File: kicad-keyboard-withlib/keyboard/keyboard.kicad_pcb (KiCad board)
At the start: 2 copper layers, 149.1 x 131.9 mm, 92 parts, among them SW1 SW_Push, SW10 SW_Push, SW11 SW_Push, SW12 SW_Push, SW13 SW_Push, SW14 SW_Push, SW15 SW_Push, SW16 SW_Push, SW17 SW_Push, SW18 SW_Push, SW19 SW_Push, SW2 SW_Push, SW20 SW_Push, SW21 SW_Push, SW22 SW_Push, SW23 SW_Push, SW24 SW_Push, SW25 SW_Push, SW26 SW_Push, SW27 SW_Push, SW28 SW_Push, SW29 SW_Push, SW3 SW_Push, SW30 SW_Push, SW31 SW_Push, SW32 SW_Push, SW33 SW_Push, SW34 SW_Push, SW35 SW_Push, SW36 SW_Push, SW37 SW_Push, SW38 SW_Push, SW39 SW_Slide_DPDT, SW4 SW_Push, SW5 SW_Push, SW6 SW_Push, SW7 SW_Push, SW8 SW_Push, SW9 SW_Push, U2 MCP23017_SO

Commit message: add:keyboardpcb almost done missing holes and homemade frogs
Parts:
- moved D30 160.6 mm to (153.0, 81.7)
- moved D38 158.6 mm to (152.2, 102.1)
- moved D19 152.4 mm to (132.6, 100.7)
- moved D20 148.1 mm to (132.6, 103.1)
- moved D18 145.6 mm to (121.4, 100.7)
- moved D17 138.4 mm to (109.8, 100.7)
- moved D28 137.1 mm to (120.2, 122.7)
- moved D29 133.4 mm to (120.4, 125.3)
- moved D27 130.9 mm to (109.6, 122.1)
- moved D36 130.2 mm to (110.2, 142.9)
- moved D37 126.8 mm to (110.2, 146.1)
- moved D26 123.9 mm to (98.0, 122.1)
- moved D35 123.4 mm to (98.8, 142.7)
- moved D25 117.1 mm to (86.8, 121.9)
- moved D34 116.9 mm to (87.6, 142.7)
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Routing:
- net Net-(U1-R1): track 175.9 -> 146.6 mm
- net Net-(U2-GPA5): track 25.9 -> 0.00 mm
- net Net-(U1-R4): track 246.4 -> 257.5 mm
- net Net-(D20-Pad1): track 0.00 -> 8.71 mm
- net Net-(D34-Pad1): track 0.00 -> 8.05 mm
- net Net-(D36-Pad1): track 0.00 -> 7.93 mm
- net Net-(D32-Pad1): track 0.00 -> 7.93 mm
- net Net-(D27-Pad1): track 0.00 -> 7.93 mm
- net Net-(D24-Pad1): track 0.00 -> 7.93 mm
- net Net-(D29-Pad1): track 0.00 -> 7.89 mm, vias 0 -> 2
- net Net-(D16-Pad1): track 0.00 -> 7.86 mm
- net Net-(D15-Pad1): track 0.00 -> 7.86 mm
- net Net-(D14-Pad1): track 0.00 -> 7.86 mm
- net Net-(D13-Pad1): track 0.00 -> 7.86 mm
- net Net-(D12-Pad1): track 0.00 -> 7.86 mm
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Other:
- board text added: "LLECIAK, MPETITCO, NROBINSO"
- board text removed: "APETITCO, LLECIAK, NROBINSO"

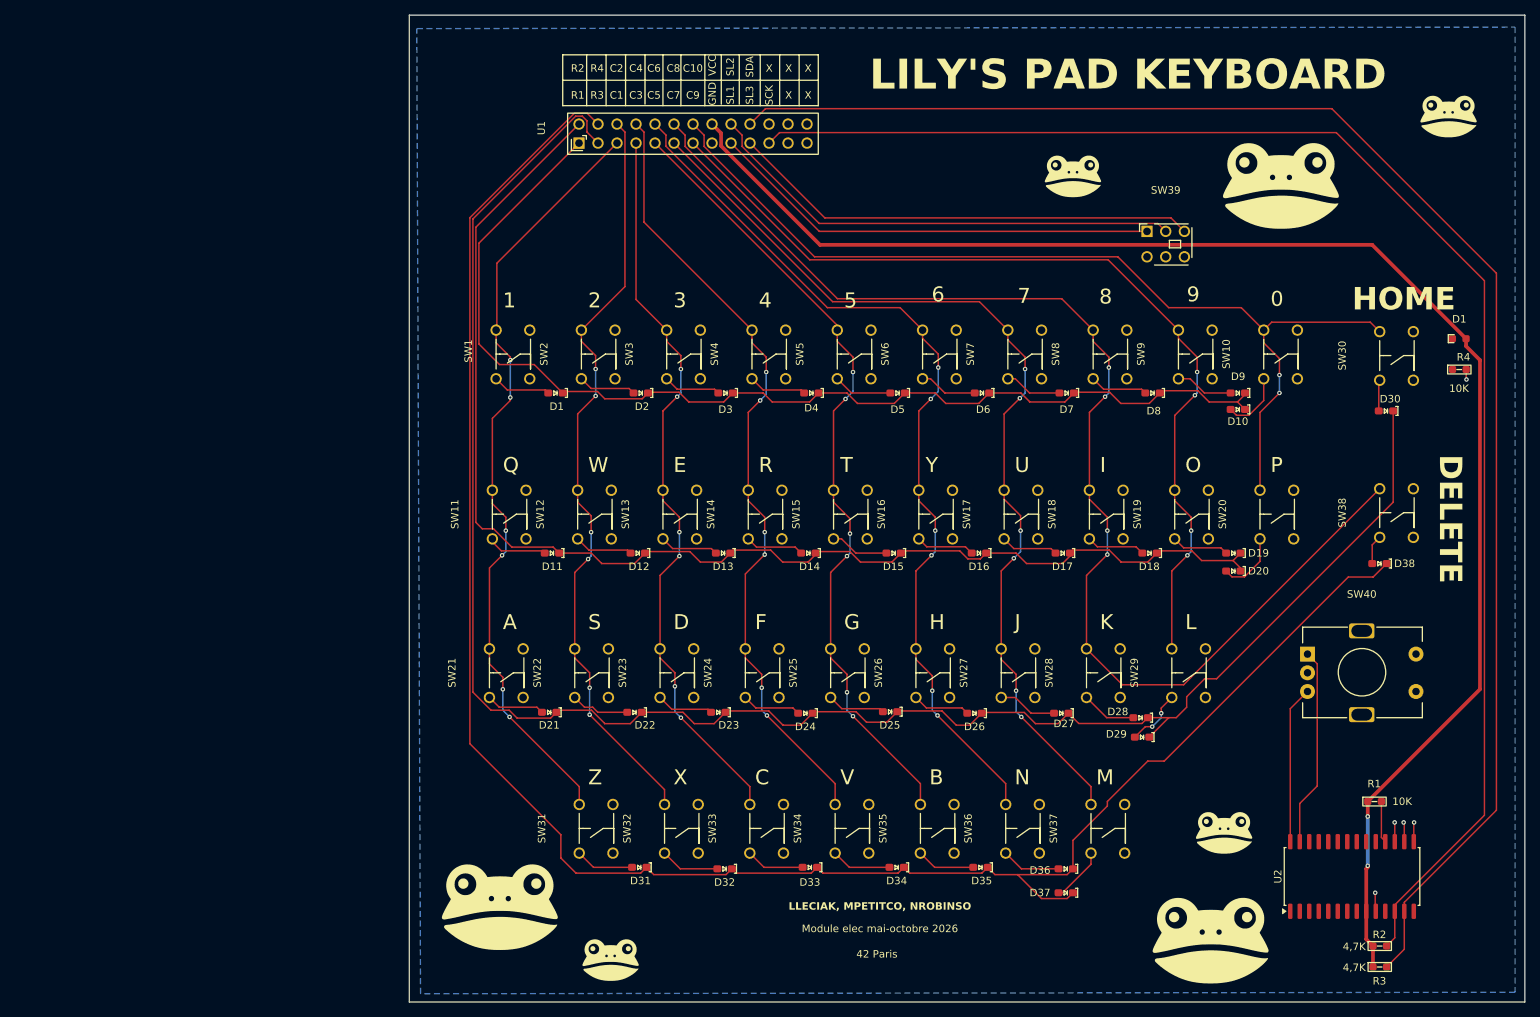
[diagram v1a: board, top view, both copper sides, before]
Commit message: add: holes in the corner of the keyboard pcb, missing homemade frogs
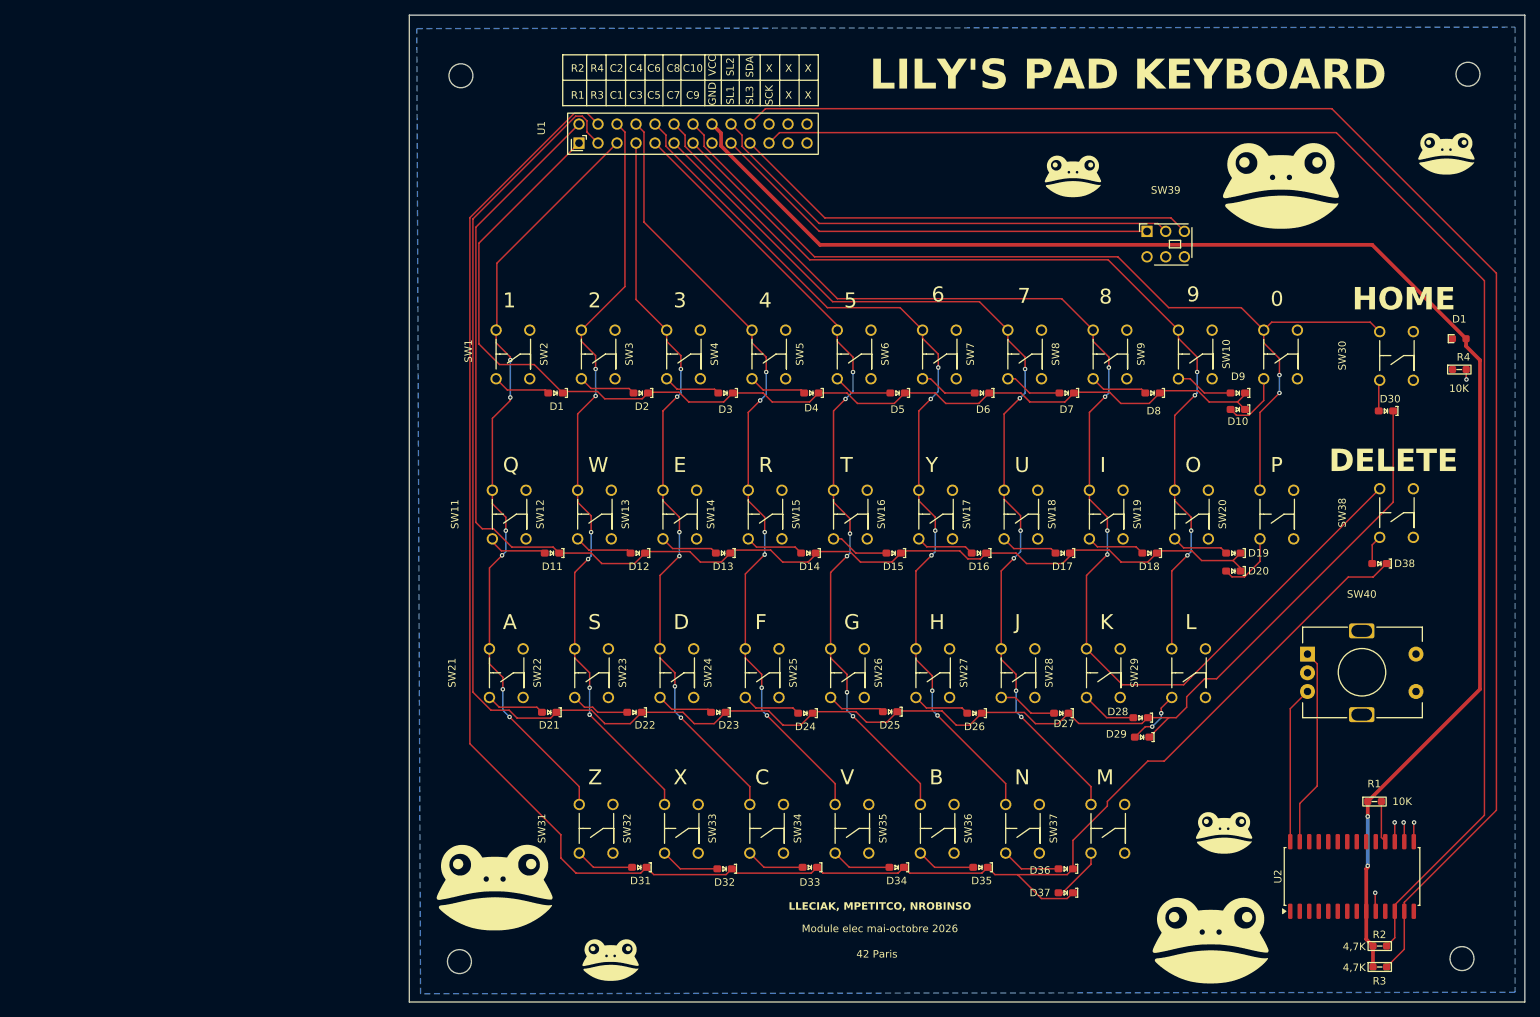
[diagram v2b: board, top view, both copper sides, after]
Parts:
- added ?: , , F.Cu at (29.2, 160.2)
- added ?: , , F.Cu at (164.0, 41.6)
- added ?: , , F.Cu at (163.2, 159.8)
- added REF**: hole, Lilyspad:hole, F.Cu at (29.3, 37.1)
- moved G*** 4.99 mm to (161.1, 51.8)
- moved G*** 2.71 mm to (33.9, 149.4)
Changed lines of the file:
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@@
 	(footprint "LOGO"
 		(layer "F.Cu")
-		(at 161.4 46.8)
+		(at 161.11282 51.782219)
 		(property "Reference" "G***"
 			(at 0 0 0)
@@
 	(footprint "LOGO"
 		(layer "F.Cu")
-		(at 34.6 152)
+		(at 33.903124 149.385094)
 		(property "Reference" "G***"
 			(at 0 0 0)
@@
 		(embedded_fonts no)
 	)
+	(footprint ""
+		(layer "F.Cu")
+		(at 29.2 160.2)
+		(property "Reference" ""
+			(at 0 0 0)
+			(layer "F.SilkS")
+			(effects
+				(font
+					(size 1.27 1.27)
+					(thickness 0.15)
+				)
+			)
+		)
+		(property "Value" ""
+			(at 0 0 0)
+			(layer "F.Fab")
+			(effects
+				(font
+					(size 1.27 1.27)
+					(thickness 0.15)
+				)
+			)
+		)
+		(property "Datasheet" ""
+			(at 0 0 0)
+			(layer "F.Fab")
+			(hide yes)
+			(effects
+				(font
+					(size 1.27 1.27)
+					(thickness 0.15)
+				)
+			)
+		)
+		(property "Description" ""
+			(at 0 0 0)
+			(layer "F.Fab")
+			(hide yes)
+			(effects
+				(font
+					(size 1.27 1.27)
+					(thickness 0.15)
+				)
+			)
+		)
+		(pad "" np_thru_hole circle
+			(at 0 0)
+			(size 3.2 3.2)
+			(drill 3.2)
+			(layers "*.Cu" "*.Mask")
+		)
+		(embedded_fonts no)
+	)
 	(footprint "LOGO"
 		(layer "F.Cu")
@@
 		(embedded_fonts no)
 	)
+	(footprint ""
+		(layer "F.Cu")
+		(at 164 41.6)
+		(property "Reference" ""
+			(at 0 0 0)
+			(layer "F.SilkS")
+			(effects
+				(font
+					(size 1.27 1.27)
+					(thickness 0.15)
+				)
+			)
+		)
+		(property "Value" ""
+			(at 0 0 0)
+			(layer "F.Fab")
+			(effects
+				(font
+					(size 1.27 1.27)
+					(thickness 0.15)
+				)
+			)
+		)
+		(property "Datasheet" ""
+			(at 0 0 0)
+			(layer "F.Fab")
+			(hide yes)
+			(effects
+				(font
+					(size 1.27 1.27)
+					(thickness 0.15)
+				)
+			)
+		)
+		(property "Description" ""
+			(at 0 0 0)
+			(layer "F.Fab")
+			(hide yes)
+			(effects
+				(font
+					(size 1.27 1.27)
+					(thickness 0.15)
+				)
+			)
+		)
+		(pad "" np_thru_hole circle
+			(at 0 0)
+			(size 3.2 3.2)
+			(drill 3.2)
+			(layers "*.Cu" "*.Mask")
+		)
+		(embedded_fonts no)
+	)
 	(footprint "LOGO"
 		(layer "F.Cu")
@@
 		(embedded_fonts no)
 	)
+	(footprint ""
+		(layer "F.Cu")
+		(at 163.2 159.8)
+		(property "Reference" ""
+			(at 0 0 0)
+			(layer "F.SilkS")
+			(effects
+				(font
+					(size 1.27 1.27)
+					(thickness 0.15)
+				)
+			)
+		)
+		(property "Value" ""
+			(at 0 0 0)
+			(layer "F.Fab")
+			(effects
+				(font
+					(size 1.27 1.27)
+					(thickness 0.15)
+				)
+			)
+		)
+		(property "Datasheet" ""
+			(at 0 0 0)
+			(layer "F.Fab")
+			(hide yes)
+			(effects
+				(font
+					(size 1.27 1.27)
+					(thickness 0.15)
+				)
+			)
+		)
+		(property "Description" ""
+			(at 0 0 0)
+			(layer "F.Fab")
+			(hide yes)
+			(effects
+				(font
+					(size 1.27 1.27)
+					(thickness 0.15)
+				)
+			)
+		)
+		(pad "" np_thru_hole circle
+			(at 0 0)
+			(size 3.2 3.2)
+			(drill 3.2)
+			(layers "*.Cu" "*.Mask")
+		)
+		(embedded_fonts no)
+	)
 	(footprint "Lilyspad:push_switch"
 		(layer "F.Cu")
@@
 		(embedded_fonts no)
 	)
+	(footprint "Lilyspad:hole"
+		(layer "F.Cu")
+		(at 29.32 37.07)
+		(property "Reference" "REF**"
+			(at 0 -0.5 0)
+			(unlocked yes)
+			(layer "F.SilkS")
+			(hide yes)
+			(effects
+				(font
+					(size 1 1)
+					(thickness 0.1)
+				)
+			)
+		)
+		(property "Value" "hole"
+			(at 0 1 0)
+			(unlocked yes)
+			(layer "F.Fab")
+			(hide yes)
+			(effects
+				(font
+					(size 1 1)
+					(thickness 0.15)
+				)
+			)
+		)
+		(property "Datasheet" ""
+			(at 0 0 0)
+			(unlocked yes)
+			(layer "F.Fab")
+			(hide yes)
+			(effects
+				(font
+					(size 1 1)
+					(thickness 0.15)
+				)
+			)
+		)
+		(property "Description" ""
+			(at 0 0 0)
+			(unlocked yes)
+			(layer "F.Fab")
+			(hide yes)
+			(effects
+				(font
+					(size 1 1)
+					(thickness 0.15)
+				)
+			)
+		)
+		(attr smd)
+		(fp_text user "${REFERENCE}"
+			(at 0 2.5 0)
+			(unlocked yes)
+			(layer "F.Fab")
+			(effects
+				(font
+					(size 1 1)
+					(thickness 0.15)
+				)
+			)
+		)
+		(pad "" np_thru_hole circle
+			(at 0.08 4.73)
+			(size 3.2 3.2)
+			(drill 3.2)
+			(layers "*.Cu" "*.Mask")
+		)
+		(embedded_fonts no)
+	)
 	(gr_line
 		(start 151.6 152.8)
@@
 	)
 	(gr_text "DELETE"
-		(at 159.8875 92.4 270)
+		(at 145.4 95 0)
 		(layer "F.SilkS")
 		(effects

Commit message: fix: no more dmca frog on keyboard pcb, made my own
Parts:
- removed the G*** at (161.1, 51.8)
- removed the G*** at (33.9, 149.4)
- removed the G*** at (139.0, 55.6)
- removed the G*** at (49.4, 159.5)
- removed the G*** at (131.4, 142.5)
- removed the G*** at (111.2, 54.8)
- removed the G*** at (129.6, 156.5)
- added G***: LOGO, LOGO, F.Cu at (118.5, 59.4)
- added G***: LOGO, LOGO, F.Cu at (50.1, 161.0)
- added G***: LOGO, LOGO, F.Cu at (143.7, 166.2)
- added G***: LOGO, LOGO, F.Cu at (140.0, 148.4)
- added G***: LOGO, LOGO, F.Cu at (168.7, 55.4)
- added G***: LOGO, LOGO, F.Cu at (154.7, 67.4)
- added G***: LOGO, LOGO, F.Cu at (53.4, 163.8)
